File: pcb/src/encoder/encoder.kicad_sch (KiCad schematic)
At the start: 9 parts, among them J1 Conn_01x05, SW1 RotaryEncoder_Switch

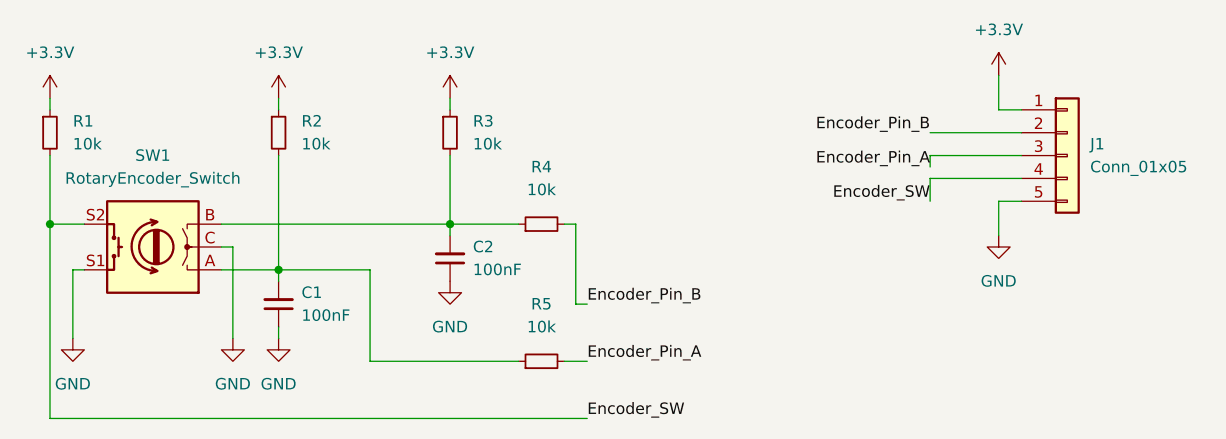
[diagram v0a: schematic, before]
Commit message: Добавил в схемы путь к репозиторию и версию. Добавил схемы в pdf.
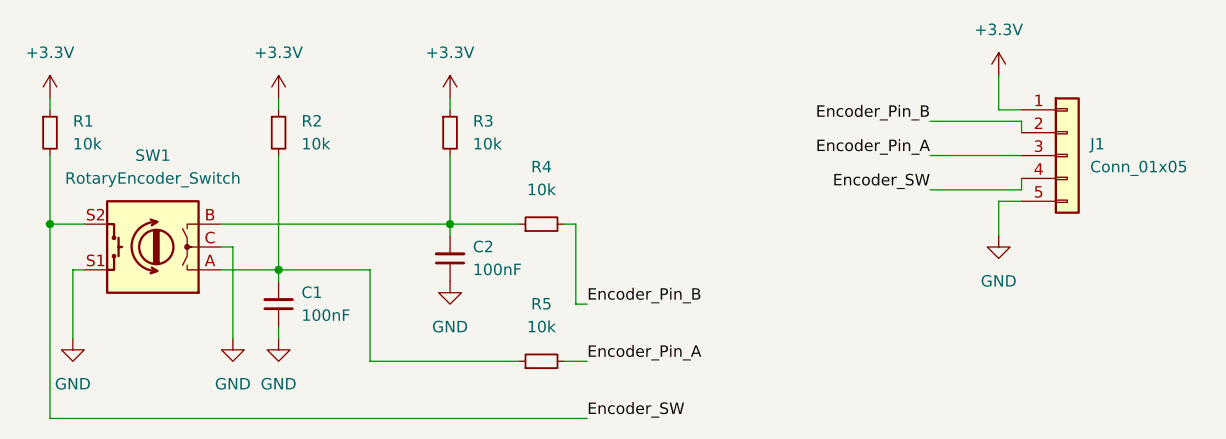
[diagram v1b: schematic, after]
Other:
- company: (none) -> Degtyarev A.
- title: (none) -> Encoder PCB
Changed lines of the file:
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@@
 (kicad_sch (version 20211123) (generator eeschema)
   (paper "A4")
+  (title_block
+    (title "Encoder PCB")
+    (date "2022-12-11")
+    (rev "1.0")
+    (company "Degtyarev A.")
+    (comment 2 "https://github.com/wb-adegtyarev/ad-modbus-encoder.git")
+  )
   (junction (at 71.12 46.99) (diameter 0) (color 0 0 0 0)
   )
@@
     (stroke (width 0) (type default) (color 0 0 0 0))
   )
-  (wire (pts (xy 134.62 41.91) (xy 124.46 41.91))
-    (stroke (width 0) (type default) (color 0 0 0 0))
-  )
   (wire (pts (xy 134.62 44.45) (xy 132.08 44.45))
     (stroke (width 0) (type default) (color 0 0 0 0))
@@
   )
   (wire (pts (xy 29.21 59.69) (xy 29.21 52.07))
-    (stroke (width 0) (type default) (color 0 0 0 0))
-  )
-  (wire (pts (xy 124.46 36.83) (xy 134.62 36.83))
-    (stroke (width 0) (type default) (color 0 0 0 0))
-  )
-  (wire (pts (xy 134.62 39.37) (xy 124.46 39.37))
     (stroke (width 0) (type default) (color 0 0 0 0))
   )
@@
     (stroke (width 0) (type default) (color 0 0 0 0))
   )
+  (wire (pts (xy 134.62 41.91) (xy 134.62 43.18))
+    (stroke (width 0) (type default) (color 0 0 0 0))
+  )
   (wire (pts (xy 71.12 46.99) (xy 71.12 48.26))
     (stroke (width 0) (type default) (color 0 0 0 0))
   )
   (wire (pts (xy 52.07 58.42) (xy 52.07 59.69))
+    (stroke (width 0) (type default) (color 0 0 0 0))
+  )
+  (wire (pts (xy 134.62 35.56) (xy 134.62 36.83))
     (stroke (width 0) (type default) (color 0 0 0 0))
   )
@@
     (stroke (width 0) (type default) (color 0 0 0 0))
   )
+  (wire (pts (xy 124.46 39.37) (xy 134.62 39.37))
+    (stroke (width 0) (type default) (color 0 0 0 0))
+  )
   (wire (pts (xy 46.99 59.69) (xy 46.99 49.53))
     (stroke (width 0) (type default) (color 0 0 0 0))
@@
     (stroke (width 0) (type default) (color 0 0 0 0))
   )
+  (wire (pts (xy 124.46 35.56) (xy 134.62 35.56))
+    (stroke (width 0) (type default) (color 0 0 0 0))
+  )
   (wire (pts (xy 26.67 33.02) (xy 26.67 34.29))
     (stroke (width 0) (type default) (color 0 0 0 0))
   )
   (wire (pts (xy 30.48 46.99) (xy 26.67 46.99))
+    (stroke (width 0) (type default) (color 0 0 0 0))
+  )
+  (wire (pts (xy 124.46 43.18) (xy 134.62 43.18))
     (stroke (width 0) (type default) (color 0 0 0 0))
   )
@@
     (stroke (width 0) (type default) (color 0 0 0 0))
   )
-  (wire (pts (xy 124.46 39.37) (xy 124.46 40.64))
-    (stroke (width 0) (type default) (color 0 0 0 0))
-  )
   (wire (pts (xy 83.82 46.99) (xy 85.09 46.99))
     (stroke (width 0) (type default) (color 0 0 0 0))
   )
   (wire (pts (xy 26.67 39.37) (xy 26.67 46.99))
-    (stroke (width 0) (type default) (color 0 0 0 0))
-  )
-  (wire (pts (xy 124.46 41.91) (xy 124.46 44.45))
     (stroke (width 0) (type default) (color 0 0 0 0))
   )
@@
     (effects (font (size 1.27 1.27)) (justify left bottom))
   )
-  (label "Encoder_SW" (at 124.46 44.45 180)
+  (label "Encoder_SW" (at 124.46 43.18 180)
     (effects (font (size 1.27 1.27)) (justify right bottom))
   )
-  (label "Encoder_Pin_A" (at 124.46 40.64 180)
+  (label "Encoder_Pin_A" (at 124.46 39.37 180)
     (effects (font (size 1.27 1.27)) (justify right bottom))
   )
-  (label "Encoder_Pin_B" (at 124.46 36.83 180)
+  (label "Encoder_Pin_B" (at 124.46 35.56 180)
     (effects (font (size 1.27 1.27)) (justify right bottom))
   )
